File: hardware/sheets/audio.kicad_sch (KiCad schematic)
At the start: 17 parts, among them J1 PicoGUS_LineIn, J2 LineOut_TRS, U1 TL072

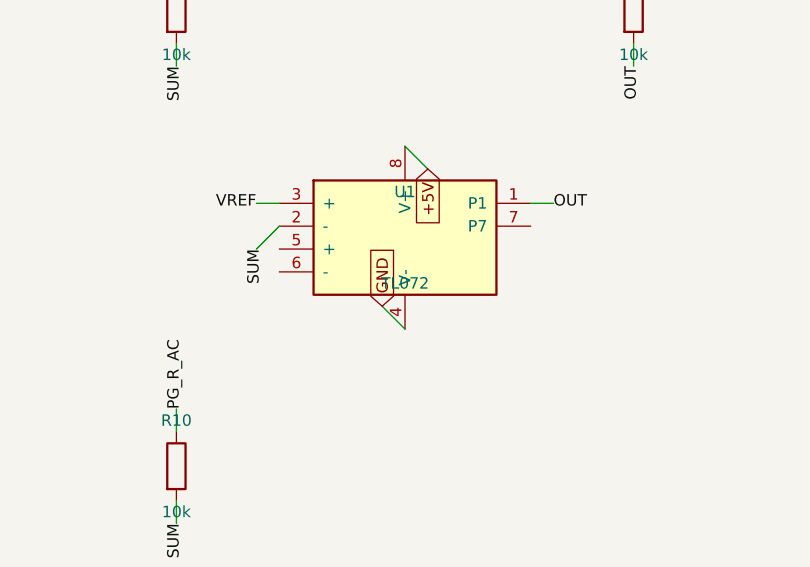
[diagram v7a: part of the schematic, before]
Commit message: Fix all critical+high design-review findings (C1-C5, H1-H8)
Full review in hardware/notes/design-review-2026-07-03.md (with per-item
fix logs). Highlights:
- SRAM strobed by gated MEMR/MEMW (was raw ~RD/~WR: I/O cycles corrupted
  SRAM and the boot shadow-load could never write it)
- Reset chain implemented: NAND combine of ~PWRGOOD + ~CPURESET drives
  V20 RESET and an always-driven RESET_DRV (dropped from the Bus MCU)
- Contention-free bus handoff: '573 OE=HLDA vs counter '244 stage
  ~OE=~HLDA; strobe gates wired + tri-stated ('125, ~OE=HLDA); Bus MCU
  address group fixed to sense; AEN/TC fixed drive; BALE input-only
- '573 LE driven by BALE (was a dangling BALE_L label)
- Data '245 DIR=DT/~R, ~OE=DEN so INTA vectors reach the CPU
- Idle pulls: strobes/DEN high, AEN/IRQ2-9/DRQ low, IOCHRDY/IOCHCK/
  DACK2-3 high
- CH224K CFG1 left open (grounding it selects 9-20V, not 5V)
- XT-IDE INTRQ pull-down (pull-up parked IRQ5 asserted)
- LPT status bit7 = ~Busy via spare inverter (SPP semantics)
- Audio summer TL072 -> MCP6002 (RRIO; TL072 out of spec at +5V single
  supply)
- card_isatest: DUT P-FET gate to V5RAW + NPN driver (default off, can
  fully turn off); /3 divider TC->~PE reload actually wired

Overturned picks corrected in notes/questions-*.md. All sheets + cards
rebuilt; structural ERC = 0; fixes netlist-verified.

Co-Authored-By: Claude Fable 5 <noreply@anthropic.com>
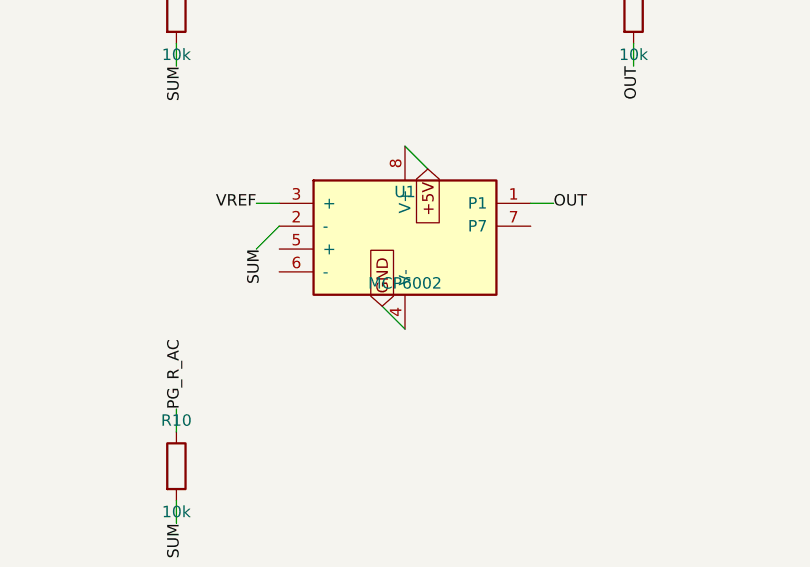
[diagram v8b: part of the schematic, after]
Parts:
- U1: value TL072 -> MCP6002
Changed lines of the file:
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@@
 		(instances
 			(project "mini-xt"
-				(path "/2e7dce83-09b2-4f89-bc6c-16aeb48854d6/4933b0aa-cf6c-4847-a136-daa0fa255efe"
+				(path "/ccbe75bb-9744-49b2-888c-84927206f4cb/667d12d6-d1e8-40d5-bea0-c1d3ff7ef318"
 					(reference "R1101")
 					(unit 1)
@@
 		(instances
 			(project "mini-xt"
-				(path "/2e7dce83-09b2-4f89-bc6c-16aeb48854d6/4933b0aa-cf6c-4847-a136-daa0fa255efe"
+				(path "/ccbe75bb-9744-49b2-888c-84927206f4cb/667d12d6-d1e8-40d5-bea0-c1d3ff7ef318"
 					(reference "R1102")
 					(unit 1)
@@
 		(instances
 			(project "mini-xt"
-				(path "/2e7dce83-09b2-4f89-bc6c-16aeb48854d6/4933b0aa-cf6c-4847-a136-daa0fa255efe"
+				(path "/ccbe75bb-9744-49b2-888c-84927206f4cb/667d12d6-d1e8-40d5-bea0-c1d3ff7ef318"
 					(reference "C1101")
 					(unit 1)
@@
 		(instances
 			(project "mini-xt"
-				(path "/2e7dce83-09b2-4f89-bc6c-16aeb48854d6/4933b0aa-cf6c-4847-a136-daa0fa255efe"
+				(path "/ccbe75bb-9744-49b2-888c-84927206f4cb/667d12d6-d1e8-40d5-bea0-c1d3ff7ef318"
 					(reference "R1103")
 					(unit 1)
@@
 		(instances
 			(project "mini-xt"
-				(path "/2e7dce83-09b2-4f89-bc6c-16aeb48854d6/4933b0aa-cf6c-4847-a136-daa0fa255efe"
+				(path "/ccbe75bb-9744-49b2-888c-84927206f4cb/667d12d6-d1e8-40d5-bea0-c1d3ff7ef318"
 					(reference "C1102")
 					(unit 1)
@@
 		(instances
 			(project "mini-xt"
-				(path "/2e7dce83-09b2-4f89-bc6c-16aeb48854d6/4933b0aa-cf6c-4847-a136-daa0fa255efe"
+				(path "/ccbe75bb-9744-49b2-888c-84927206f4cb/667d12d6-d1e8-40d5-bea0-c1d3ff7ef318"
 					(reference "C1103")
 					(unit 1)
@@
 		(instances
 			(project "mini-xt"
-				(path "/2e7dce83-09b2-4f89-bc6c-16aeb48854d6/4933b0aa-cf6c-4847-a136-daa0fa255efe"
+				(path "/ccbe75bb-9744-49b2-888c-84927206f4cb/667d12d6-d1e8-40d5-bea0-c1d3ff7ef318"
 					(reference "J1101")
 					(unit 1)
@@
 		(instances
 			(project "mini-xt"
-				(path "/2e7dce83-09b2-4f89-bc6c-16aeb48854d6/4933b0aa-cf6c-4847-a136-daa0fa255efe"
+				(path "/ccbe75bb-9744-49b2-888c-84927206f4cb/667d12d6-d1e8-40d5-bea0-c1d3ff7ef318"
 					(reference "C1104")
 					(unit 1)
@@
 		(instances
 			(project "mini-xt"
-				(path "/2e7dce83-09b2-4f89-bc6c-16aeb48854d6/4933b0aa-cf6c-4847-a136-daa0fa255efe"
+				(path "/ccbe75bb-9744-49b2-888c-84927206f4cb/667d12d6-d1e8-40d5-bea0-c1d3ff7ef318"
 					(reference "C1105")
 					(unit 1)
@@
 			)
 		)
-		(property "Value" "TL072"
+		(property "Value" "MCP6002"
 			(at 177.8 157.48 0)
 			(effects
@@
 		(instances
 			(project "mini-xt"
-				(path "/2e7dce83-09b2-4f89-bc6c-16aeb48854d6/4933b0aa-cf6c-4847-a136-daa0fa255efe"
+				(path "/ccbe75bb-9744-49b2-888c-84927206f4cb/667d12d6-d1e8-40d5-bea0-c1d3ff7ef318"
 					(reference "U1101")
 					(unit 1)
@@
 		(instances
 			(project "mini-xt"
-				(path "/2e7dce83-09b2-4f89-bc6c-16aeb48854d6/4933b0aa-cf6c-4847-a136-daa0fa255efe"
+				(path "/ccbe75bb-9744-49b2-888c-84927206f4cb/667d12d6-d1e8-40d5-bea0-c1d3ff7ef318"
 					(reference "C1106")
 					(unit 1)
@@
 		(instances
 			(project "mini-xt"
-				(path "/2e7dce83-09b2-4f89-bc6c-16aeb48854d6/4933b0aa-cf6c-4847-a136-daa0fa255efe"
+				(path "/ccbe75bb-9744-49b2-888c-84927206f4cb/667d12d6-d1e8-40d5-bea0-c1d3ff7ef318"
 					(reference "R1104")
 					(unit 1)
@@
 		(instances
 			(project "mini-xt"
-				(path "/2e7dce83-09b2-4f89-bc6c-16aeb48854d6/4933b0aa-cf6c-4847-a136-daa0fa255efe"
+				(path "/ccbe75bb-9744-49b2-888c-84927206f4cb/667d12d6-d1e8-40d5-bea0-c1d3ff7ef318"
 					(reference "R1105")
 					(unit 1)
@@
 		(instances
 			(project "mini-xt"
-				(path "/2e7dce83-09b2-4f89-bc6c-16aeb48854d6/4933b0aa-cf6c-4847-a136-daa0fa255efe"
+				(path "/ccbe75bb-9744-49b2-888c-84927206f4cb/667d12d6-d1e8-40d5-bea0-c1d3ff7ef318"
 					(reference "R1110")
 					(unit 1)
@@
 		(instances
 			(project "mini-xt"
-				(path "/2e7dce83-09b2-4f89-bc6c-16aeb48854d6/4933b0aa-cf6c-4847-a136-daa0fa255efe"
+				(path "/ccbe75bb-9744-49b2-888c-84927206f4cb/667d12d6-d1e8-40d5-bea0-c1d3ff7ef318"
 					(reference "R1106")
 					(unit 1)
@@
 		(instances
 			(project "mini-xt"
-				(path "/2e7dce83-09b2-4f89-bc6c-16aeb48854d6/4933b0aa-cf6c-4847-a136-daa0fa255efe"
+				(path "/ccbe75bb-9744-49b2-888c-84927206f4cb/667d12d6-d1e8-40d5-bea0-c1d3ff7ef318"
 					(reference "C1107")
 					(unit 1)
@@
 		(instances
 			(project "mini-xt"
-				(path "/2e7dce83-09b2-4f89-bc6c-16aeb48854d6/4933b0aa-cf6c-4847-a136-daa0fa255efe"
+				(path "/ccbe75bb-9744-49b2-888c-84927206f4cb/667d12d6-d1e8-40d5-bea0-c1d3ff7ef318"
 					(reference "J1102")
 					(unit 1)
